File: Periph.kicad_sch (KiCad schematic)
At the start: 17 parts, among them J4 SM04B-GHS-TB, U10 ICM-42688-P, U11 BMP388, U9 W25Q128JVSIQ

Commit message: PumbaaV2_RC2
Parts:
- C28, C29: footprint Capacitor_SMD:C_0201_0603Metric -> Capacitor_SMD:C_0402_1005Metric; LCSC Part # (none) -> C1525
- J4: value SM04B-GHS-TB -> SM04B-GHS-TB(LF)(SN)
- LSE1: LCSC Part  C2650753 -> C2650753 C5280579
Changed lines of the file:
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@@
-	(symbol
-		(lib_id "Device:C_Small")
-		(at 215.9 45.72 90)
-		(unit 1)
-		(exclude_from_sim no)
-		(in_bom yes)
-		(on_board yes)
-		(dnp no)
-		(fields_autoplaced yes)
-		(property "Reference" "C28"
-			(at 215.9063 39.37 90)
-			(effects
-				(font
-					(size 1.27 1.27)
-				)
-			)
-		)
-		(property "Value" "100n"
-			(at 215.9063 41.91 90)
-			(effects
-				(font
-					(size 1.27 1.27)
-				)
-			)
-		)
-		(property "Footprint" "Capacitor_SMD:C_0201_0603Metric"
-			(at 215.9 45.72 0)
-			(effects
-				(font
-					(size 1.27 1.27)
-				)
-				(hide yes)
-			)
-		)
-		(property "Datasheet" "~"
-			(at 215.9 45.72 0)
-			(effects
-				(font
-					(size 1.27 1.27)
-				)
-				(hide yes)
-			)
-		)
-		(property "Description" ""
-			(at 215.9 45.72 0)
-			(effects
-				(font
-					(size 1.27 1.27)
-				)
-			)
-		)
-		(pin "1"
-		)
-		(pin "2"
-		)
-		(instances
-			(project "MX_IMU"
-				(path "/8ed38441-7d4e-4e89-870f-07e11c6dce38/57f4b5bf-da86-4b65-9b05-7c9ef99c472c"
-					(reference "C28")
-					(unit 1)
-				)
-			)
-		)
-	)
 	(symbol
 		(lib_id "Device:C_Small")
@@
 			)
 		)
-		(property "Value" "SM04B-GHS-TB"
+		(property "Value" "SM04B-GHS-TB(LF)(SN)"
 			(at 209.55 91.4399 0)
 			(effects
@@
 	)
 	(symbol
+		(lib_id "Device:C_Small")
+		(at 237.49 46.99 90)
+		(unit 1)
+		(exclude_from_sim no)
+		(in_bom yes)
+		(on_board yes)
+		(dnp no)
+		(property "Reference" "C29"
+			(at 234.95 40.64 90)
+			(effects
+				(font
+					(size 1.27 1.27)
+				)
+				(justify right)
+			)
+		)
+		(property "Value" "100n"
+			(at 234.95 43.18 90)
+			(effects
+				(font
+					(size 1.27 1.27)
+				)
+				(justify right)
+			)
+		)
+		(property "Footprint" "Capacitor_SMD:C_0402_1005Metric"
+			(at 237.49 46.99 0)
+			(effects
+				(font
+					(size 1.27 1.27)
+				)
+				(hide yes)
+			)
+		)
+		(property "Datasheet" "~"
+			(at 237.49 46.99 0)
+			(effects
+				(font
+					(size 1.27 1.27)
+				)
+				(hide yes)
+			)
+		)
+		(property "Description" ""
+			(at 237.49 46.99 0)
+			(effects
+				(font
+					(size 1.27 1.27)
+				)
+			)
+		)
+		(property "LCSC Part #" "C1525"
+			(at 237.49 46.99 0)
+			(effects
+				(font
+					(size 1.27 1.27)
+				)
+				(hide yes)
+			)
+		)
+		(pin "2"
+		)
+		(pin "1"
+		)
+		(instances
+			(project "MX_IMU"
+				(path "/8ed38441-7d4e-4e89-870f-07e11c6dce38/57f4b5bf-da86-4b65-9b05-7c9ef99c472c"
+					(reference "C29")
+					(unit 1)
+				)
+			)
+		)
+	)
+	(symbol
 		(lib_id "power:+3.3V")
 		(at 186.69 53.34 0)
@@
 			)
 		)
-		(property "LCSC Part " "C2650753"
+		(property "LCSC Part " "C2650753  C5280579"
 			(at 82.55 38.1 0)
 			(effects
@@
 				(path "/8ed38441-7d4e-4e89-870f-07e11c6dce38/57f4b5bf-da86-4b65-9b05-7c9ef99c472c"
 					(reference "LSE1")
-					(unit 1)
-				)
-			)
-		)
-	)
-	(symbol
-		(lib_id "Device:C_Small")
-		(at 237.49 46.99 90)
-		(unit 1)
-		(exclude_from_sim no)
-		(in_bom yes)
-		(on_board yes)
-		(dnp no)
-		(fields_autoplaced yes)
-		(property "Reference" "C29"
-			(at 237.4963 40.64 90)
-			(effects
-				(font
-					(size 1.27 1.27)
-				)
-			)
-		)
-		(property "Value" "100n"
-			(at 237.4963 43.18 90)
-			(effects
-				(font
-					(size 1.27 1.27)
-				)
-			)
-		)
-		(property "Footprint" "Capacitor_SMD:C_0201_0603Metric"
-			(at 237.49 46.99 0)
-			(effects
-				(font
-					(size 1.27 1.27)
-				)
-				(hide yes)
-			)
-		)
-		(property "Datasheet" "~"
-			(at 237.49 46.99 0)
-			(effects
-				(font
-					(size 1.27 1.27)
-				)
-				(hide yes)
-			)
-		)
-		(property "Description" ""
-			(at 237.49 46.99 0)
-			(effects
-				(font
-					(size 1.27 1.27)
-				)
-			)
-		)
-		(pin "1"
-		)
-		(pin "2"
-		)
-		(instances
-			(project "MX_IMU"
-				(path "/8ed38441-7d4e-4e89-870f-07e11c6dce38/57f4b5bf-da86-4b65-9b05-7c9ef99c472c"
-					(reference "C29")
 					(unit 1)
 				)
@@
 					(unit 1)
 				)
+			)
+		)
+	)
+	(symbol
+		(lib_id "Device:C_Small")
+		(at 215.9 45.72 90)
+		(unit 1)
+		(exclude_from_sim no)
+		(in_bom yes)
+		(on_board yes)
+		(dnp no)
+		(property "Reference" "C28"
+			(at 213.36 39.37 90)
+			(effects
+				(font
+					(size 1.27 1.27)
+				)
+				(justify right)
+			)
+		)
+		(property "Value" "100n"
+			(at 213.36 41.91 90)
+			(effects
+				(font
+					(size 1.27 1.27)
+				)
+				(justify right)
+			)
+		)
+		(property "Footprint" "Capacitor_SMD:C_0402_1005Metric"
+			(at 215.9 45.72 0)
+			(effects
+				(font
+					(size 1.27 1.27)
+				)
+				(hide yes)
+			)
+		)
+		(property "Datasheet" "~"
+			(at 215.9 45.72 0)
+			(effects
+				(font
+					(size 1.27 1.27)
+				)
+				(hide yes)
+			)
+		)
+		(property "Description" ""
+			(at 215.9 45.72 0)
+			(effects
+				(font
+					(size 1.27 1.27)
+				)
+			)
+		)
+		(property "LCSC Part #" "C1525"
+			(at 215.9 45.72 0)
+			(effects
+				(font
+					(size 1.27 1.27)
+				)
+				(hide yes)
+			)
+		)
+		(pin "2"
+		)
+		(pin "1"
+		)
+		(instances
+			(project "MX_IMU"
+				(path "/8ed38441-7d4e-4e89-870f-07e11c6dce38/57f4b5bf-da86-4b65-9b05-7c9ef99c472c"
+					(reference "C28")
+					(unit 1)
+				)

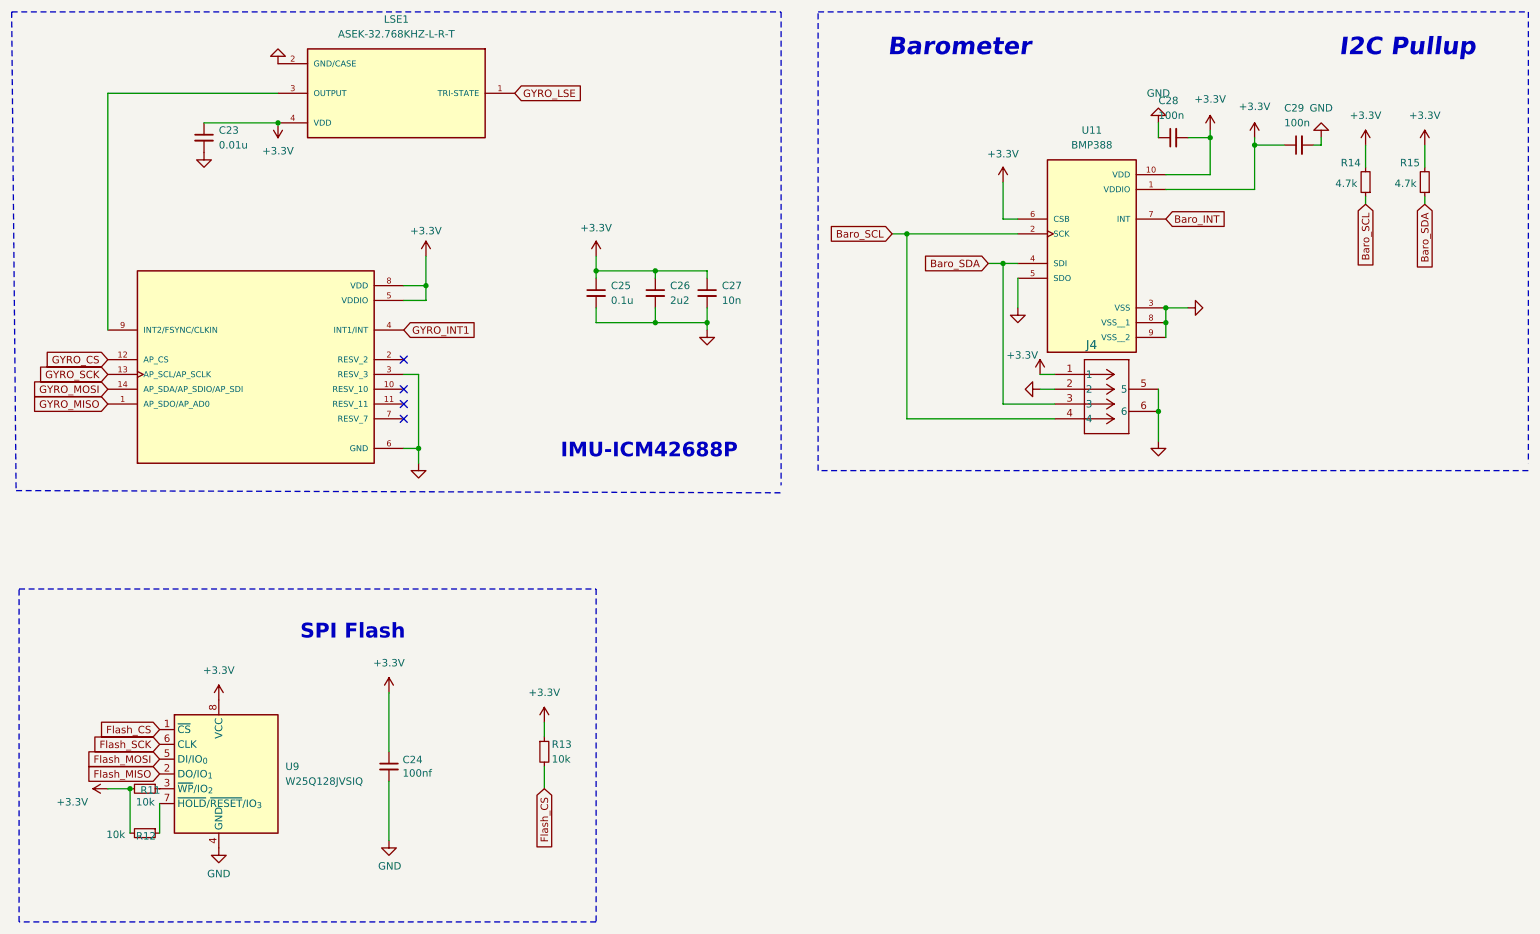
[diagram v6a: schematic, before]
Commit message: compact  IMU module for integration
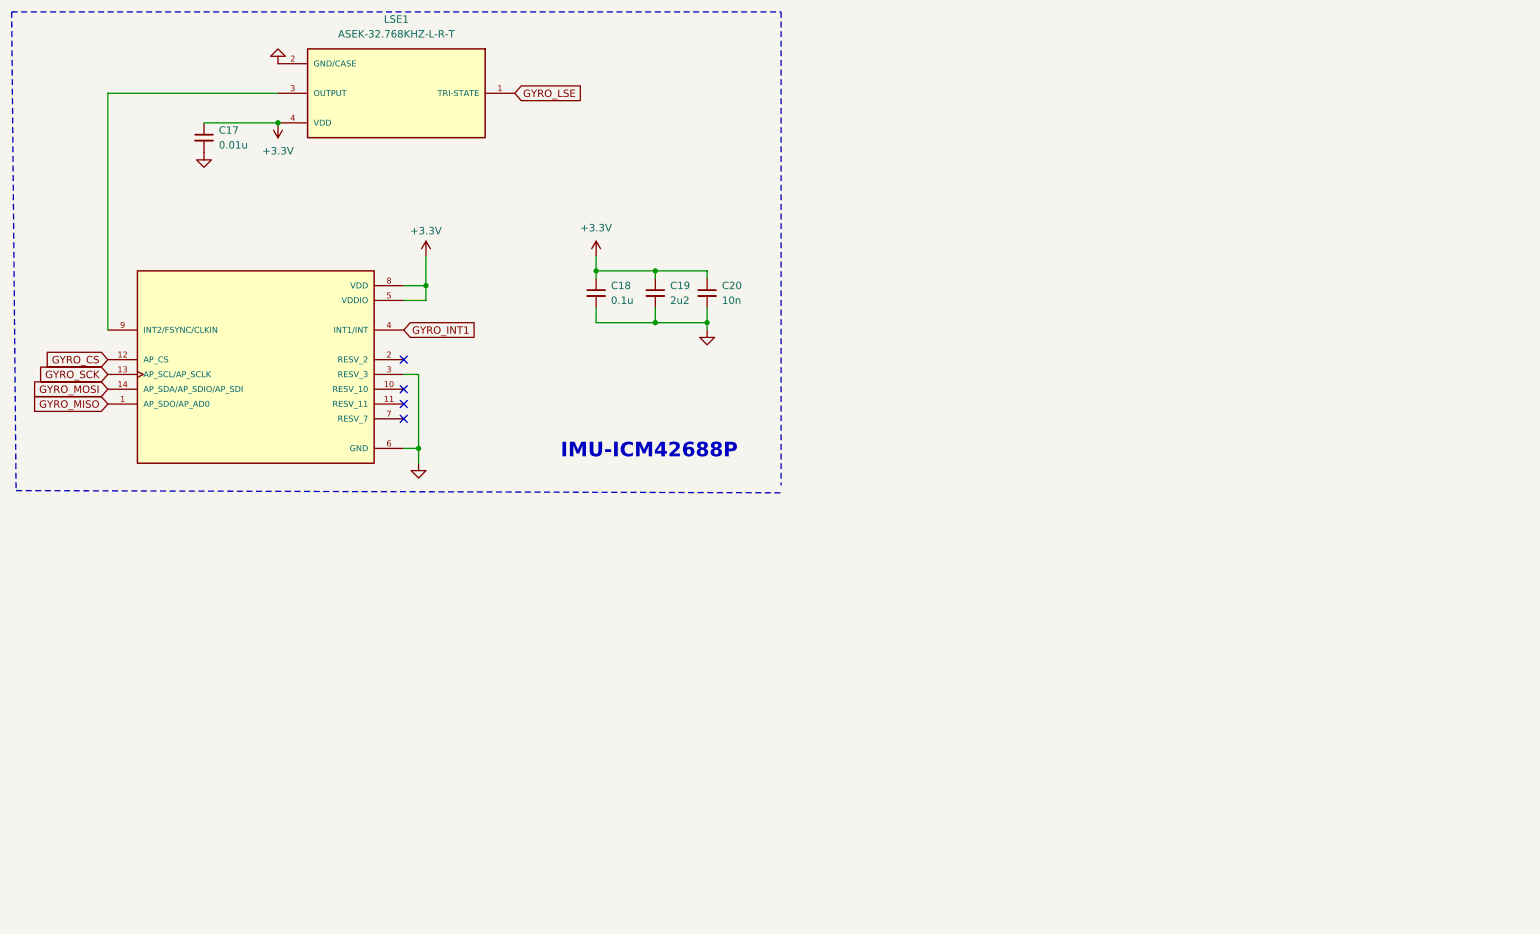
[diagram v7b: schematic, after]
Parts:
- removed C24: 100nf, Capacitor_SMD:C_0603_1608Metric, symbol Device:C_Small
- removed C28, C29: 100n, Capacitor_SMD:C_0402_1005Metric, symbol Device:C_Small
- removed J4: SM04B-GHS-TB(LF)(SN), mylib:CONN_SM04B-GHS-TB_JST, symbol SM04B-GHS-TB:SM04B-GHS-TB
- removed R11, R12, R13: 10k, Resistor_SMD:R_0402_1005Metric, symbol Device:R_Small
- removed R14, R15: 4.7k, Resistor_SMD:R_0603_1608Metric, symbol Device:R_Small
- removed U11: BMP388, mylib:BMP388, symbol BMP388:BMP388
- removed U9: W25Q128JVSIQ, Package_SO:SOIC-8_5.3x5.3mm_P1.27mm, symbol Memory_Flash:W25Q128JVS
- renumbered C23 to C17, C25 to C18, C26 to C19, C27 to C20, U10 to U6
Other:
- note removed: "Barometer"
- note removed: "I2C Pullup"
- note removed: "SPI Flash"
